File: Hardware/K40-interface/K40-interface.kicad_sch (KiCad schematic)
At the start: 14 parts, among them P1 CONN_01X08, P2 CONN_01X04, P3 CONN_01X04, P4 CONN_01X04, P5 CONN_01X04, U1 4049, U2 4N25

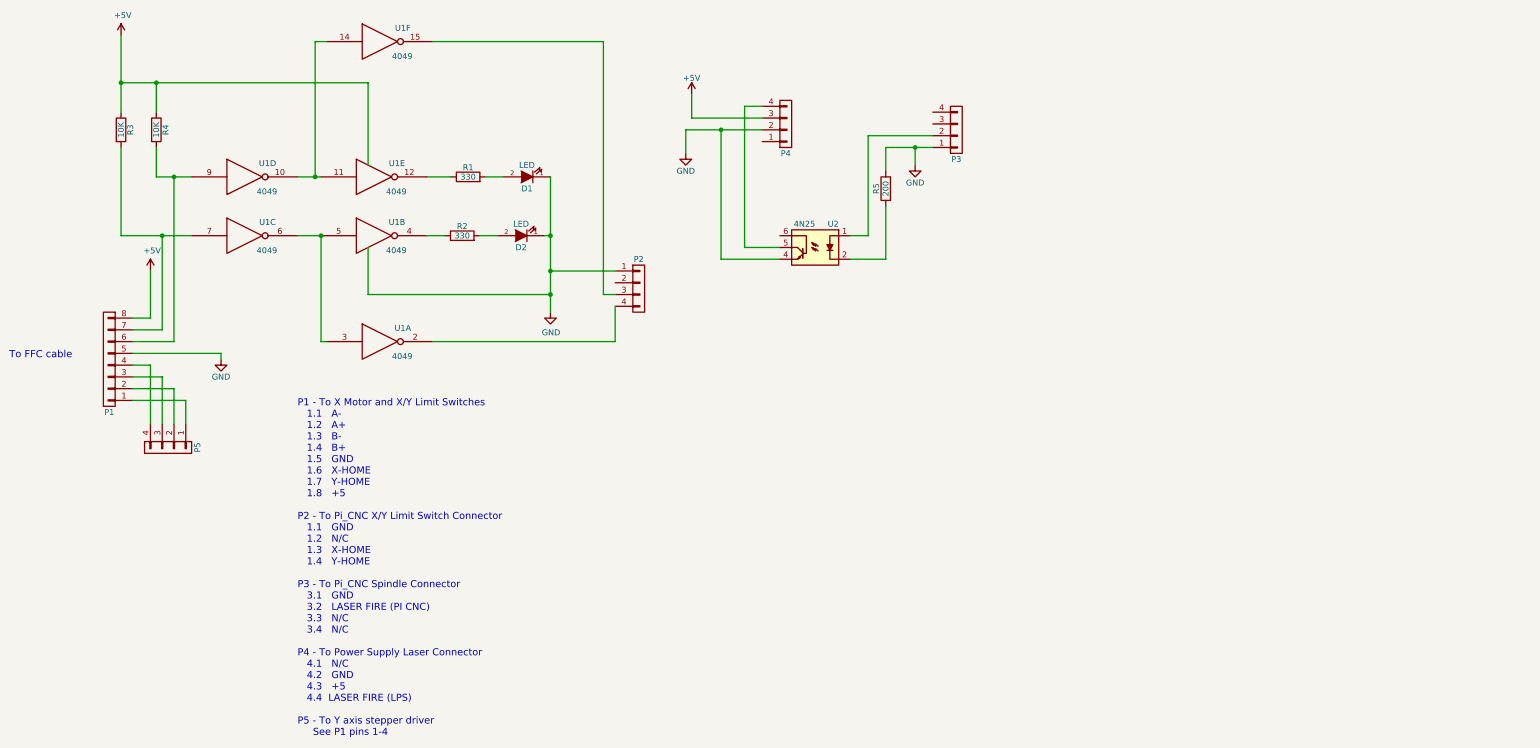
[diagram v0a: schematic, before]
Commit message: Changes to interface PCB layout - test
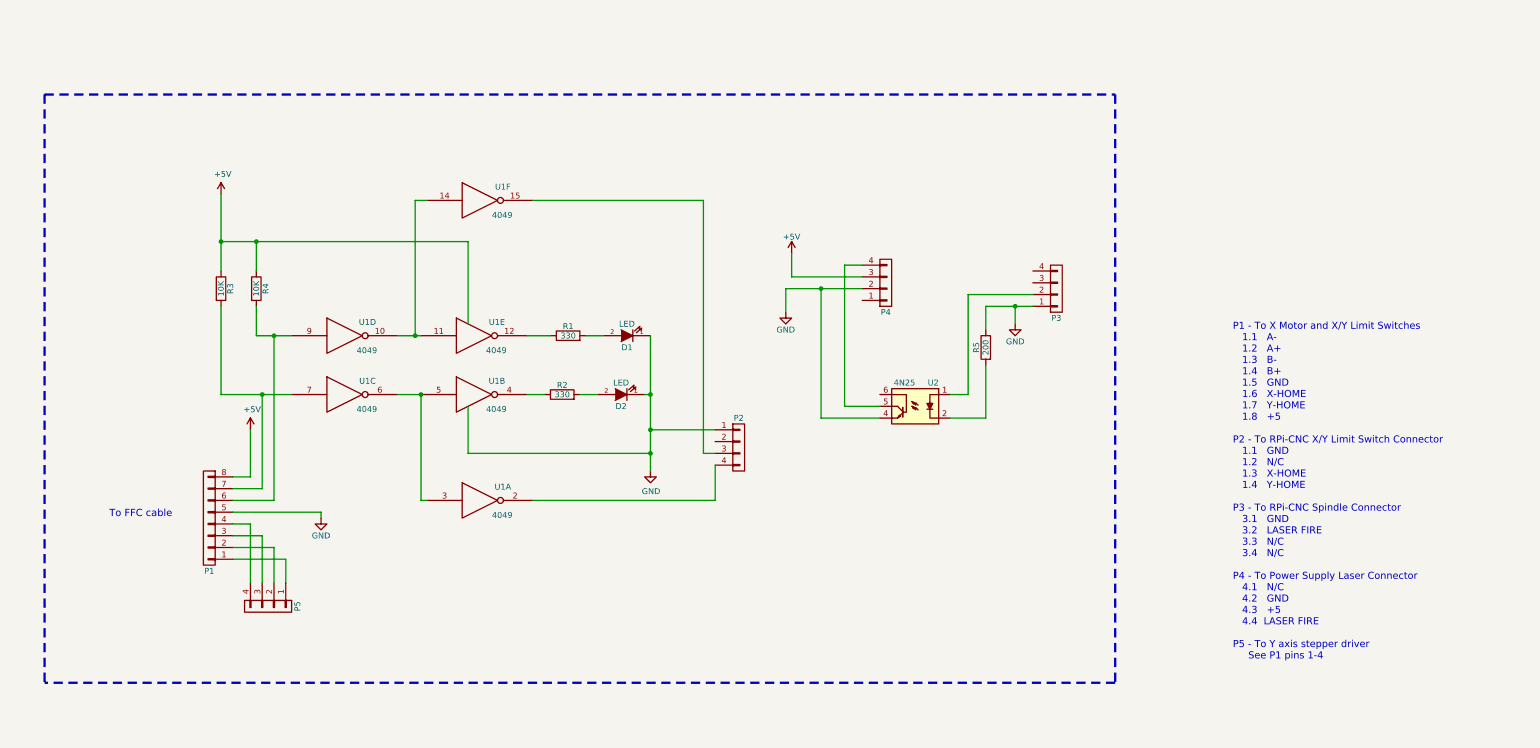
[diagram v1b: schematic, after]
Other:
- note added: "P1 - To X Motor and X/Y Limit Switches 1.1 A- 1.2 A+ 1.3 B- 1.4 B+ 1.5 GND 1.6 X-HOME 1.7 Y-HOME 1.8 +5 P2 - To RPi-CNC X/Y Limit Switch Connector 1.1 GND 1.2 N/C 1.3 X-HOME 1.4 Y-HOME P3 - To RPi-CNC Spindle Connector 3.1 GND 3.2 LASER FIRE 3.3 N/C 3.4 N/C P4 - To Power Supply Laser Connector 4.1 N/C 4.2 GND 4.3 +5 4.4 LASER FIRE P5 - To Y axis stepper driver See P1 pins 1-4"
- note removed: "P1 - To X Motor and X/Y Limit Switches 1.1 A- 1.2 A+ 1.3 B- 1.4 B+ 1.5 GND 1.6 X-HOME 1.7 Y-HOME 1.8 +5 P2 - To Pi_CNC X/Y Limit Switch Connector 1.1 GND 1.2 N/C 1.3 X-HOME 1.4 Y-HOME P3 - To Pi_CNC Spindle Connector 3.1 GND 3.2 LASER FIRE (PI CNC) 3.3 N/C 3.4 N/C P4 - To Power Supply Laser Connector 4.1 N/C 4.2 GND 4.3 +5 4.4 LASER FIRE (LPS) P5 - To Y axis stepper driver See P1 pins 1-4"
- moved on the sheet: D1, D2, P1, P2, P3, P4, P5, R1, R2, R3, R4, R5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
